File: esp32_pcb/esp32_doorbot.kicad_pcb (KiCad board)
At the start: 2 copper layers, 30 x 23.1 mm, 16 parts, among them J2 Conn_01x02_Female, J3 Conn_01x08, J4 Conn_01x06, Q1 2N7002E, U1 L7805, U2 74LVC2T45DC

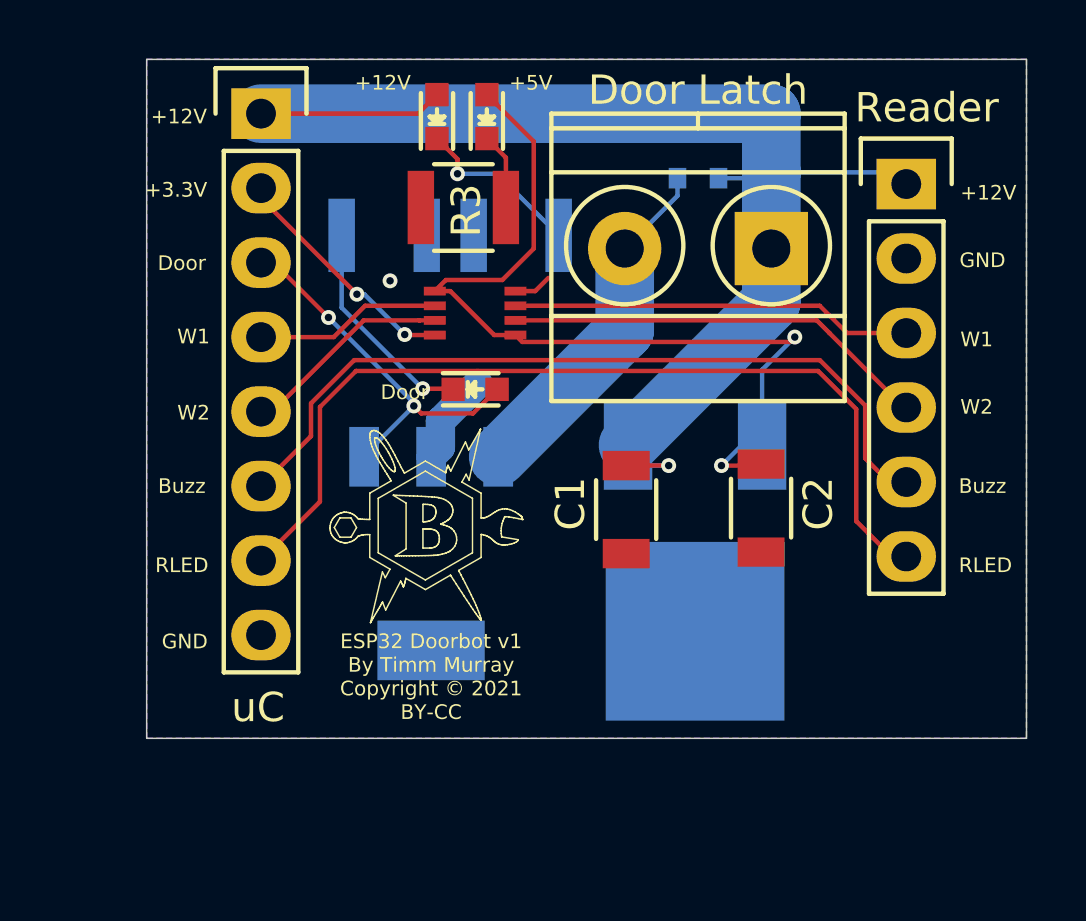
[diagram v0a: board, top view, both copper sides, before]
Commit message: Use header that attaches to wesp32 board directly
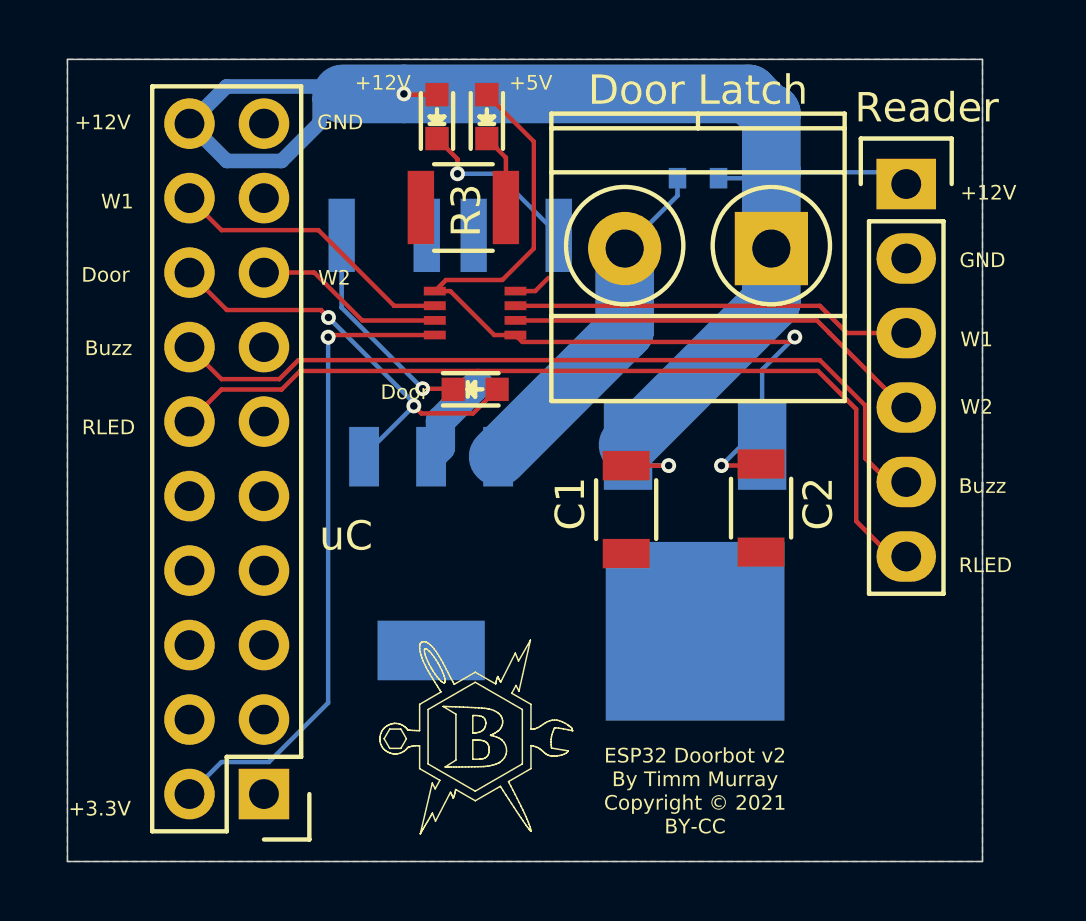
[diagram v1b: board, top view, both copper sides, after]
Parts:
- J3: value Conn_01x08 -> ESP32; footprint Pin_Headers:Pin_Header_Straight_1x08 -> Pin_Headers:Pin_Header_Straight_2x10
- moved J3 23.2 mm to (134.4, 103.7), turned to 180 degrees
- moved REF** 7.40 mm to (141.7, 105.3)
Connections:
- J3 pad 1: 12V -> Net-(J3-Pad1)
- J3 pad 3: DOOR -> Net-(J3-Pad3)
- J3 pad 4: WIEGAND_OUT1 -> Net-(J3-Pad4)
- J3 pad 5: WIEGAND_OUT2 -> Net-(J3-Pad5)
- J3 pad 6: READER_BUZZ -> Net-(J3-Pad6)
- J3 pad 7: READER_LED -> Net-(J3-Pad7)
- J3 pad 8: GND -> Net-(J3-Pad8)
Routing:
- net 3.3V: track 8.20 -> 22.2 mm, vias 2 -> 1
- net 12V: track 46.8 -> 51.4 mm, vias 1 -> 2
- net WIEGAND_OUT1: track 6.37 -> 9.89 mm
- net DOOR: track 13.0 -> 15.3 mm
- net READER_LED: track 31.4 -> 30.0 mm
- net READER_BUZZ: track 27.2 -> 27.9 mm
- net WIEGAND_OUT2: track 7.21 -> 6.50 mm
- net GND: vias 1 -> 0
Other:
- board size 30 x 23.1 mm -> 31.2 x 27.3 mm
- board text added: "ESP32 Doorbot v2 By Timm Murray Copyright © 2021 BY-CC"
- board text removed: "ESP32 Doorbot v1 By Timm Murray Copyright © 2021 BY-CC"

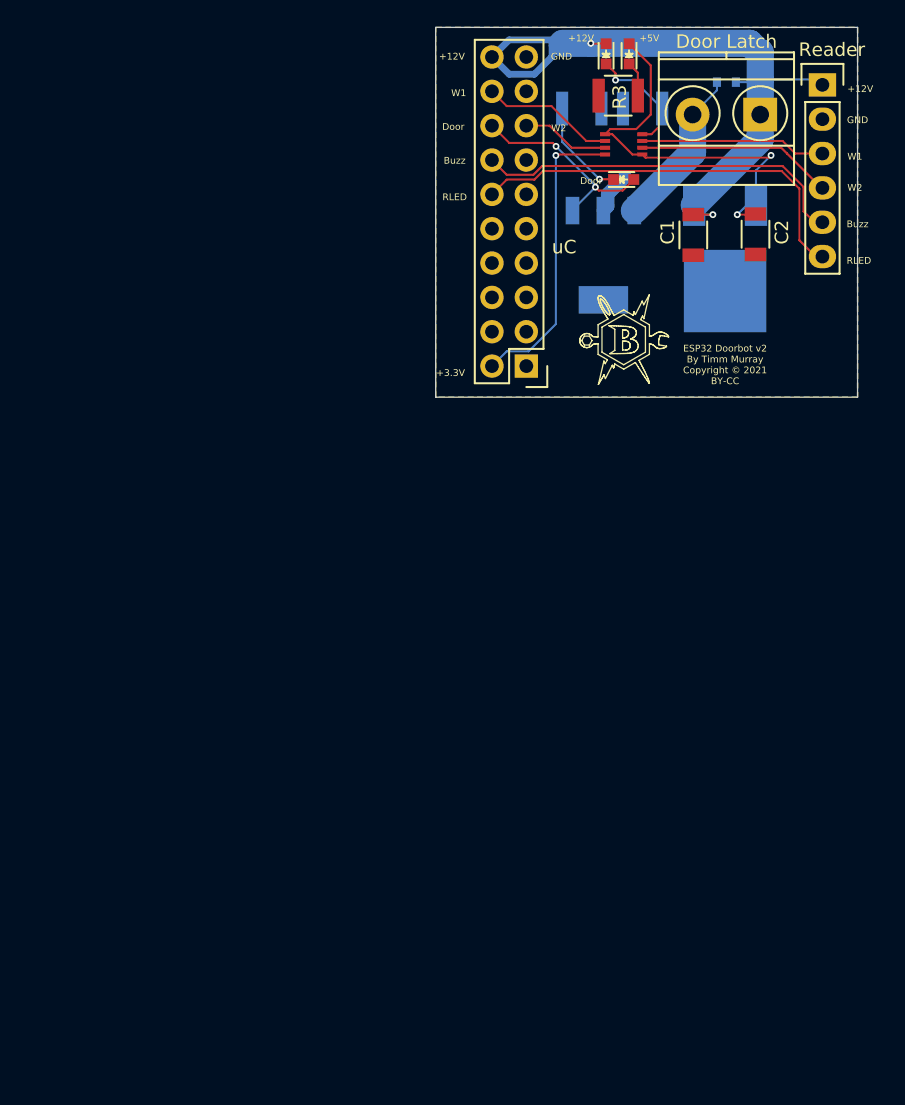
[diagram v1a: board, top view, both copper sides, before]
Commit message: New layout for regular esp32
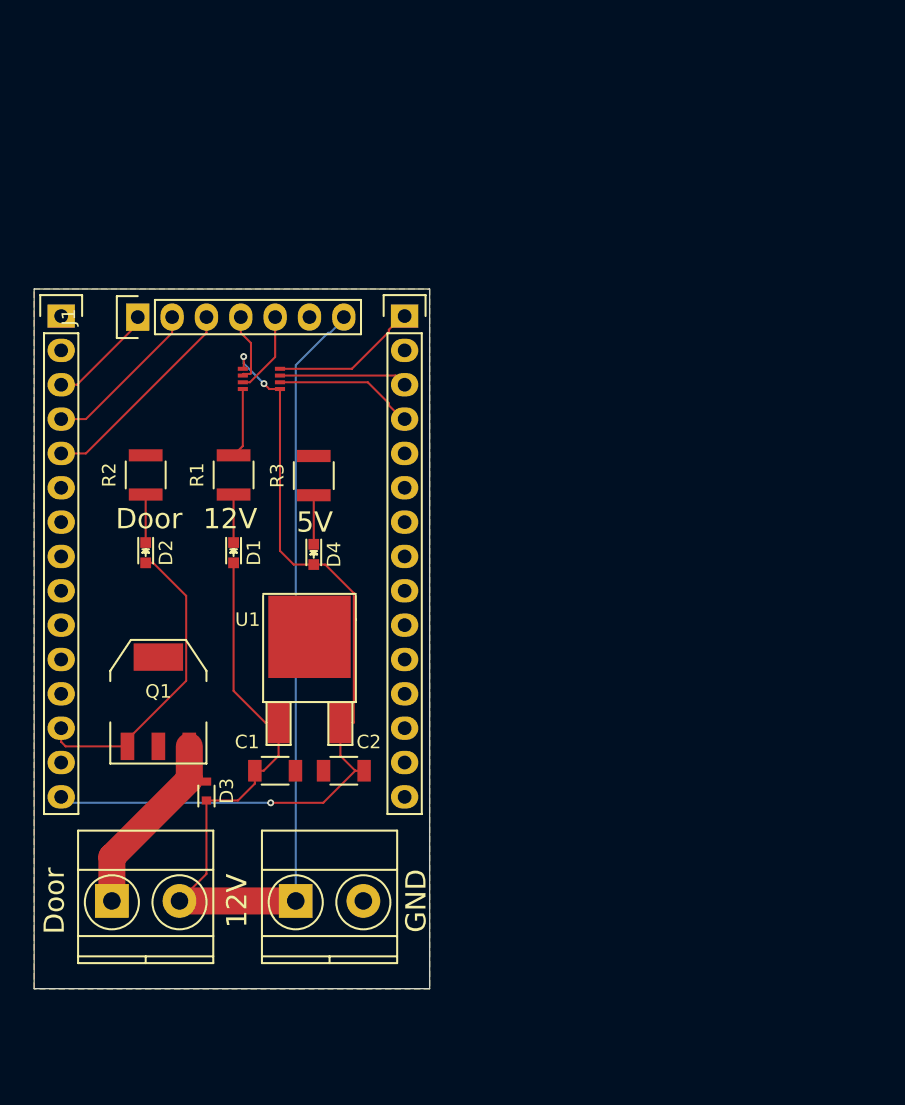
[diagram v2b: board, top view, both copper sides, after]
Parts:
- added J1: Conn_01x07_Male, Pin_Headers:Pin_Header_Straight_1x07, F.Cu at (105.7, 100.1)
- added J5: WROOM32_2, Pin_Headers:Pin_Header_Straight_1x15, F.Cu at (125.4, 100.0)
- D1, D2, D4: footprint LEDs:LED-0603 -> LEDs:LED_0603
- D3, Q1, R1, R2, U1: moved to F.Cu
- J3: value ESP32 -> Barrel_Jack; footprint Pin_Headers:Pin_Header_Straight_2x10 -> Terminal_Blocks:TerminalBlock_Pheonix_MKDS1.5-2pol
- J4: value Conn_01x06 -> WROOM32_1; footprint Pin_Headers:Pin_Header_Straight_1x06 -> Pin_Headers:Pin_Header_Straight_1x15
- REF**: moved to B.Cu
- U2: footprint Tinkerforge-kicad:VSSOP8 -> tinkerforge-kicad:VSSOP8
- moved J2 75.4 mm to (103.8, 143.3), turned to 0 degrees
- moved D3 65.0 mm to (110.7, 135.1), turned to 270 degrees
- moved J4 58.8 mm to (100.0, 100.0)
- moved C1 50.3 mm to (115.8, 133.6), turned to 0 degrees
- moved C2 50.0 mm to (120.9, 133.6), turned to 180 degrees
- moved U1 49.1 mm to (118.4, 130.1)
- moved Q1 46.6 mm to (107.2, 128.5)
- moved D1 46.1 mm to (112.8, 117.5), turned to 270 degrees
- moved D2 44.8 mm to (106.2, 117.5), turned to 270 degrees
- moved D4 43.8 mm to (118.7, 117.6), turned to 270 degrees
- moved J3 43.1 mm to (117.3, 143.3), turned to 0 degrees
- moved R2 42.1 mm to (106.2, 111.8), turned to 90 degrees
- moved R1 40.6 mm to (112.8, 111.8), turned to 90 degrees
- moved R3 36.0 mm to (118.7, 111.8), turned to 90 degrees
- moved REF** 35.5 mm to (106.2, 105.2)
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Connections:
- J2 pad 1: 12V -> LATCH_OUT
- J2 pad 2: LATCH_OUT -> 12V
- J3 pad 1: Net-(J3-Pad1) -> 12V
- J3 pad 2: 3.3V -> GND
- J4 pad 1: 12V -> (no net)
- J4 pad 2: GND -> (no net)
- J4 pad 3: WIEGAND_IN1 -> 24_32_SWITCH
- J4 pad 4: WIEGAND_IN2 -> READER_LED
- J4 pad 6: READER_LED -> (no net)
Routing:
- net 12V: track 51.4 -> 85.1 mm, vias 2 -> 0
- net 5V: track 30.1 -> 61.8 mm, vias 2 -> 3
- net READER_LED: track 30.0 -> 12.0 mm
- net READER_BUZZ: track 27.9 -> 15.6 mm
- net 3.3V: track 22.2 -> 10.9 mm, vias 1 -> 0
- net WIEGAND_IN2: track 15.3 -> 5.19 mm
- net 24_32_SWITCH: track 0.00 -> 8.03 mm
- net DOOR: track 15.3 -> 23.0 mm, vias 2 -> 0
- net WIEGAND_IN1: track 13.7 -> 6.12 mm
- net LATCH_OUT: track 12.0 -> 16.3 mm
- net Net-(D2-Pad1): track 7.42 -> 3.55 mm, vias 1 -> 0
- net WIEGAND_OUT2: track 6.50 -> 9.50 mm
- net Net-(D1-Pad1): track 6.02 -> 3.55 mm, vias 1 -> 0
- net GND: track 4.47 -> 5.19 mm
- net WIEGAND_OUT1: track 9.89 -> 10.4 mm
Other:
- board size 31.2 x 27.3 mm -> 29.2 x 51.8 mm
- board text added: "12V"
- board text added: "5V"
- board text added: "ESP32 Doorbot v3 By Timm Murray Copyright © 2021 BY-CC"
- board text removed: "+12V"
- board text removed: "+3.3V"
- board text removed: "+5V"
- board text removed: "Buzz"
- board text removed: "Door Latch"
- board text removed: "ESP32 Doorbot v2 By Timm Murray Copyright © 2021 BY-CC"
- board text removed: "RLED"
- board text removed: "Reader"
- board text removed: "W1"
- board text removed: "W2"
- board text removed: "uC"

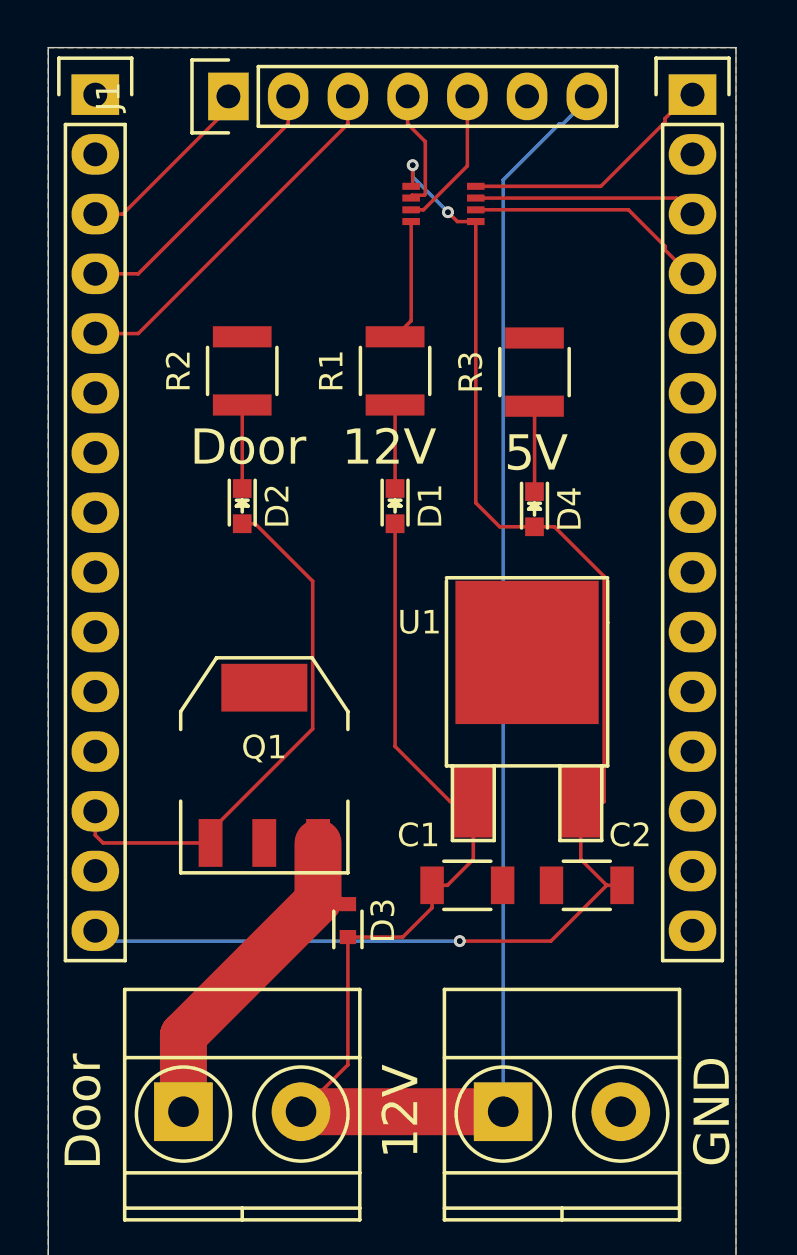
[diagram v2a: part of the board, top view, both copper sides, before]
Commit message: Use larger components. Correct pinout and spacing
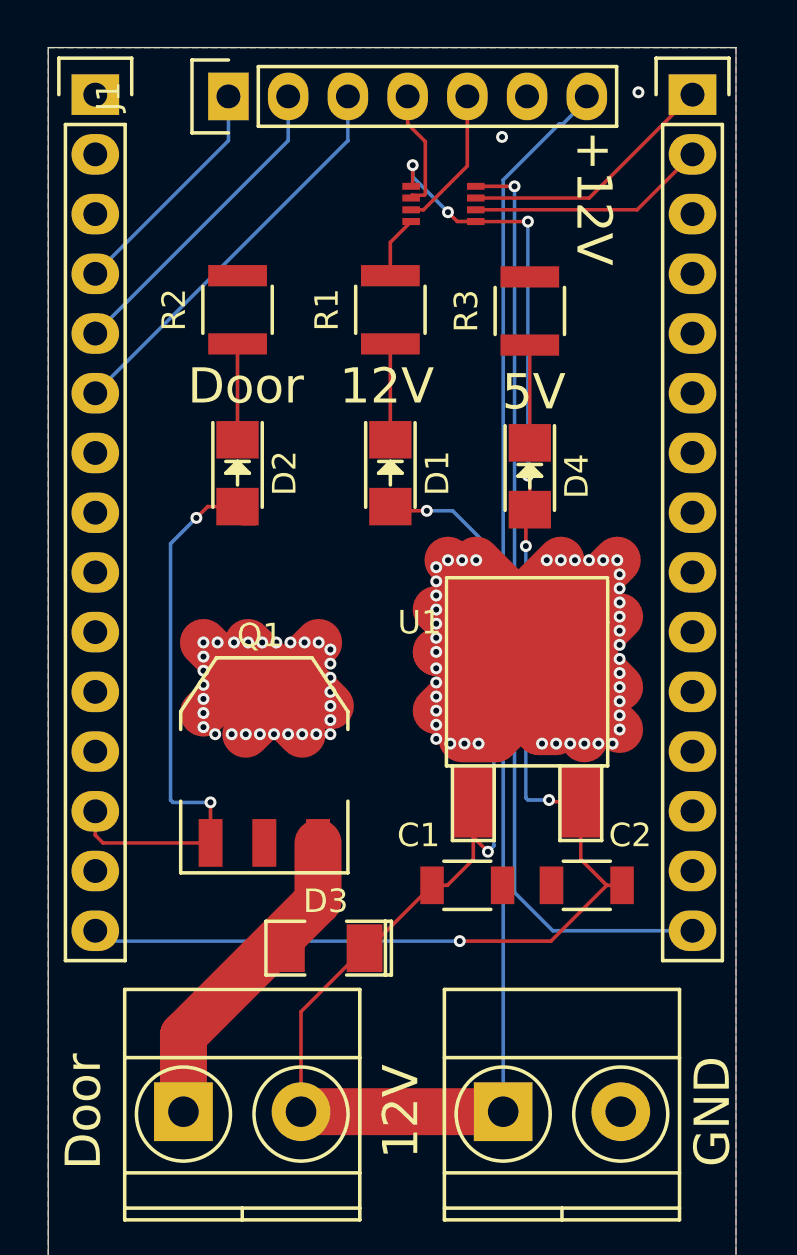
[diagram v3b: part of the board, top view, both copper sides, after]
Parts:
- D1, D2, D4: footprint LEDs:LED_0603 -> LEDs:LED-1206
- D3: footprint Diodes_SMD:SOD-523 -> SMD_Packages:SMD-1206_Pol
- moved R1 2.61 mm to (112.5, 109.2)
- moved R2 2.61 mm to (106.0, 109.2)
- moved R3 2.61 mm to (118.5, 109.2)
- moved D3 1.50 mm to (109.8, 136.3), turned to 180 degrees
- moved D1 1.41 mm to (112.5, 116.1)
- moved D2 1.41 mm to (106.0, 116.1)
- moved D4 1.41 mm to (118.5, 116.2)
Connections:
- J4 pad 1: (no net) -> Net-(J4-Pad1)
- J4 pad 10: (no net) -> Net-(J4-Pad10)
- J4 pad 11: (no net) -> Net-(J4-Pad11)
- J4 pad 12: (no net) -> Net-(J4-Pad12)
- J4 pad 2: (no net) -> Net-(J4-Pad2)
- J4 pad 3: 24_32_SWITCH -> Net-(J4-Pad3)
- J4 pad 4: READER_LED -> 24_32_SWITCH
- J4 pad 5: READER_BUZZ -> READER_LED
- J4 pad 6: (no net) -> READER_BUZZ
- J4 pad 7: (no net) -> Net-(J4-Pad7)
- J4 pad 8: (no net) -> Net-(J4-Pad8)
- J4 pad 9: (no net) -> Net-(J4-Pad9)
- J5 pad 1: 3.3V -> WIEGAND_OUT2
- J5 pad 10: (no net) -> Net-(J5-Pad10)
- J5 pad 11: (no net) -> Net-(J5-Pad11)
- J5 pad 12: (no net) -> Net-(J5-Pad12)
- J5 pad 13: (no net) -> Net-(J5-Pad13)
- J5 pad 14: (no net) -> GND
- J5 pad 15: (no net) -> 3.3V
- J5 pad 2: (no net) -> WIEGAND_OUT1
- J5 pad 3: WIEGAND_OUT2 -> Net-(J5-Pad3)
- J5 pad 4: WIEGAND_OUT1 -> Net-(J5-Pad4)
- J5 pad 5: (no net) -> Net-(J5-Pad5)
- J5 pad 6: (no net) -> Net-(J5-Pad6)
- J5 pad 7: (no net) -> Net-(J5-Pad7)
- J5 pad 8: (no net) -> Net-(J5-Pad8)
- J5 pad 9: (no net) -> Net-(J5-Pad9)
- Q1 pad 4: (no net) -> GND
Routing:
- net GND: track 5.19 -> 85.1 mm, vias 0 -> 75
- net 3.3V: track 10.9 -> 39.9 mm, vias 0 -> 1
- net 12V: track 85.1 -> 90.5 mm, vias 0 -> 2
- net 24_32_SWITCH: track 8.03 -> 10.4 mm
- net DOOR: track 23.0 -> 25.0 mm, vias 0 -> 2
- net WIEGAND_OUT2: track 9.50 -> 11.0 mm
- net READER_BUZZ: track 15.6 -> 17.1 mm
- net READER_LED: track 12.0 -> 13.5 mm
- net LATCH_OUT: track 16.3 -> 15.2 mm
- net Net-(D2-Pad1): track 3.55 -> 4.08 mm
- net Net-(D1-Pad1): track 3.55 -> 4.08 mm
- net Net-(D4-Pad1): track 3.63 -> 4.16 mm
- net 5V: track 61.8 -> 61.7 mm, vias 3 -> 7
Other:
- board text added: "+12V"
